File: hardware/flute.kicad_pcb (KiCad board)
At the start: 2 copper layers, 280 x 20 mm, 30 parts, among them J1 Conn_01x04, SW1 C, SW2 D, SW3 E, SW4 F, SW5 G, SW6 A, SW7 H, SW8 OCTAVE?, U1 W25Q128JVS, Y1 Crystal_GND24

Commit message: Update flute.kicad_pcb
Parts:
- MIC.CASE1: moved to B.Cu
- moved MIC.CASE1 57.4 mm to (73.5, 101.5), turned to -90 degrees
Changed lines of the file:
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@@
 		)
 	)
-	(footprint "Resistor_THT:R_Axial_DIN0204_L3.6mm_D1.6mm_P2.54mm_Vertical"
-		(layer "F.Cu")
-		(at 61.695 45.36)
-		(descr "Resistor, Axial_DIN0204 series, Axial, Vertical, pin pitch=2.54mm, 0.167W, length*diameter=3.6*1.6mm^2, http://cdn-reichelt.de/documents/datenblatt/B400/1_4W%23YAG.pdf")
-		(tags "Resistor Axial_DIN0204 series Axial Vertical pin pitch 2.54mm 0.167W length 3.6mm diameter 1.6mm")
-		(property "Reference" "MIC.CASE1"
-			(at 1.27 -1.92 0)
-			(layer "F.SilkS")
-			(effects
-				(font
-					(size 1 1)
-					(thickness 0.15)
-				)
-			)
-		)
-		(property "Value" "R"
-			(at 1.27 1.92 0)
-			(layer "F.Fab")
-			(effects
-				(font
-					(size 1 1)
-					(thickness 0.15)
-				)
-			)
-		)
-		(property "Datasheet" "~"
-			(at 0 0 0)
-			(layer "F.Fab")
-			(hide yes)
-			(effects
-				(font
-					(size 1.27 1.27)
-					(thickness 0.15)
-				)
-			)
-		)
-		(property "Description" "Resistor"
-			(at 0 0 0)
-			(layer "F.Fab")
-			(hide yes)
-			(effects
-				(font
-					(size 1.27 1.27)
-					(thickness 0.15)
-				)
-			)
-		)
-		(property ki_fp_filters "R_*")
-		(sheetname "/MICROPHONE/")
-		(sheetfile "./microphone.kicad_sch")
-		(attr through_hole)
-		(fp_line
-			(start 0.92 0)
-			(end 1.54 0)
-			(stroke
-				(width 0.12)
-				(type solid)
-			)
-			(layer "F.SilkS")
-		)
-		(fp_circle
-			(center 0 0)
-			(end 0.92 0)
-			(stroke
-				(width 0.12)
-				(type solid)
-			)
-			(fill no)
-			(layer "F.SilkS")
-		)
-		(fp_rect
-			(start -1.05 -1.05)
-			(end 3.49 1.05)
-			(stroke
-				(width 0.05)
-				(type solid)
-			)
-			(fill no)
-			(layer "F.CrtYd")
-		)
-		(fp_line
-			(start 0 0)
-			(end 2.54 0)
-			(stroke
-				(width 0.1)
-				(type solid)
-			)
-			(layer "F.Fab")
-		)
-		(fp_circle
-			(center 0 0)
-			(end 0.8 0)
-			(stroke
-				(width 0.1)
-				(type solid)
-			)
-			(fill no)
-			(layer "F.Fab")
-		)
-		(fp_text user "${REFERENCE}"
-			(at 1.27 -1.92 0)
-			(layer "F.Fab")
-			(effects
-				(font
-					(size 1 1)
-					(thickness 0.15)
-				)
-			)
-		)
-		(pad "1" thru_hole circle
-			(at 0 0)
-			(size 1.4 1.4)
-			(drill 0.7)
-			(layers "*.Cu" "*.Mask")
-			(remove_unused_layers no)
-			(net 3 "GND")
-			(pintype "passive")
-		)
-		(pad "2" thru_hole circle
-			(at 2.54 0)
-			(size 1.4 1.4)
-			(drill 0.7)
-			(layers "*.Cu" "*.Mask")
-			(remove_unused_layers no)
-			(net 2 "Net-(C1-Pad1)")
-			(pintype "passive")
-		)
-		(embedded_fonts no)
-		(model "${KICAD9_3DMODEL_DIR}/Resistor_THT.3dshapes/R_Axial_DIN0204_L3.6mm_D1.6mm_P2.54mm_Vertical.step"
-			(offset
-				(xyz 0 0 0)
-			)
-			(scale
-				(xyz 1 1 1)
-			)
-			(rotate
-				(xyz 0 0 0)
-			)
-		)
-	)
 	(footprint "Button_Switch_SMD:SW_SPST_Omron_B3FS-100xP"
 		(layer "F.Cu")
@@
 			(offset
 				(xyz 0 0 0)
+			)
+			(scale
+				(xyz 1 1 1)
+			)
+			(rotate
+				(xyz 0 0 0)
+			)
+		)
+	)
+	(footprint "Resistor_THT:R_Axial_DIN0204_L3.6mm_D1.6mm_P2.54mm_Vertical"
+		(layer "B.Cu")
+		(at 73.46 101.5 -90)
+		(descr "Resistor, Axial_DIN0204 series, Axial, Vertical, pin pitch=2.54mm, 0.167W, length*diameter=3.6*1.6mm^2, http://cdn-reichelt.de/documents/datenblatt/B400/1_4W%23YAG.pdf")
+		(tags "Resistor Axial_DIN0204 series Axial Vertical pin pitch 2.54mm 0.167W length 3.6mm diameter 1.6mm")
+		(property "Reference" "MIC.CASE1"
+			(at 1.27 1.92 90)
+			(layer "B.SilkS")
+			(effects
+				(font
+					(size 1 1)
+					(thickness 0.15)
+				)
+				(justify mirror)
+			)
+		)
+		(property "Value" "R"
+			(at 1.27 -1.92 90)
+			(layer "B.Fab")
+			(effects
+				(font
+					(size 1 1)
+					(thickness 0.15)
+				)
+				(justify mirror)
+			)
+		)
+		(property "Datasheet" "~"
+			(at 0 0 90)
+			(layer "B.Fab")
+			(hide yes)
+			(effects
+				(font
+					(size 1.27 1.27)
+					(thickness 0.15)
+				)
+				(justify mirror)
+			)
+		)
+		(property "Description" "Resistor"
+			(at 0 0 90)
+			(layer "B.Fab")
+			(hide yes)
+			(effects
+				(font
+					(size 1.27 1.27)
+					(thickness 0.15)
+				)
+				(justify mirror)
+			)
+		)
+		(property ki_fp_filters "R_*")
+		(sheetname "/MICROPHONE/")
+		(sheetfile "./microphone.kicad_sch")
+		(attr through_hole)
+		(fp_line
+			(start 0.92 0)
+			(end 1.54 0)
+			(stroke
+				(width 0.12)
+				(type solid)
+			)
+			(layer "B.SilkS")
+		)
+		(fp_circle
+			(center 0 0)
+			(end 0.92 0)
+			(stroke
+				(width 0.12)
+				(type solid)
+			)
+			(fill no)
+			(layer "B.SilkS")
+		)
+		(fp_rect
+			(start -1.05 1.05)
+			(end 3.49 -1.05)
+			(stroke
+				(width 0.05)
+				(type solid)
+			)
+			(fill no)
+			(layer "B.CrtYd")
+		)
+		(fp_line
+			(start 0 0)
+			(end 2.54 0)
+			(stroke
+				(width 0.1)
+				(type solid)
+			)
+			(layer "B.Fab")
+		)
+		(fp_circle
+			(center 0 0)
+			(end 0.8 0)
+			(stroke
+				(width 0.1)
+				(type solid)
+			)
+			(fill no)
+			(layer "B.Fab")
+		)
+		(fp_text user "${REFERENCE}"
+			(at 1.27 1.92 90)
+			(layer "B.Fab")
+			(effects
+				(font
+					(size 1 1)
+					(thickness 0.15)
+				)
+				(justify mirror)
+			)
+		)
+		(pad "1" thru_hole circle
+			(at 0 0 270)
+			(size 1.4 1.4)
+			(drill 0.7)
+			(layers "*.Cu" "*.Mask")
+			(remove_unused_layers no)
+			(net 3 "GND")
+			(pintype "passive")
+		)
+		(pad "2" thru_hole circle
+			(at 2.54 0 270)
+			(size 1.4 1.4)
+			(drill 0.7)
+			(layers "*.Cu" "*.Mask")
+			(remove_unused_layers no)
+			(net 2 "Net-(C1-Pad1)")
+			(pintype "passive")
+		)
+		(embedded_fonts no)
+		(model "${KICAD9_3DMODEL_DIR}/Resistor_THT.3dshapes/R_Axial_DIN0204_L3.6mm_D1.6mm_P2.54mm_Vertical.step"
+			(offset
+				(xyz 0 0 0)

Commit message: Update flute.kicad_pcb
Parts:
- moved C1 82.5 mm to (67.0, 130.2), turned to 90 degrees
- moved R1 82.2 mm to (67.7, 131.5)
- moved MIC.CASE1 28.6 mm to (65.5, 129.0)
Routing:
- net Net-(C1-Pad1): track 0.00 -> 3.02 mm
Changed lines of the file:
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@@
 	(footprint "Resistor_SMD:R_0201_0603Metric"
 		(layer "F.Cu")
-		(at 61.345 49.56)
+		(at 67.655 131.5)
 		(descr "Resistor SMD 0201 (0603 Metric), square (rectangular) end terminal, IPC-7351 nominal, (Body size source: https://www.vishay.com/docs/20052/crcw0201e3.pdf), generated with kicad-footprint-generator")
 		(tags "resistor")
@@
 	(footprint "Capacitor_SMD:C_0201_0603Metric"
 		(layer "F.Cu")
-		(at 61.345 47.81)
+		(at 67 130.155 90)
 		(descr "Capacitor SMD 0201 (0603 Metric), square (rectangular) end terminal, IPC-7351 nominal, (Body size source: https://www.vishay.com/docs/20052/crcw0201e3.pdf), generated with kicad-footprint-generator")
 		(tags "capacitor")
 		(property "Reference" "C1"
-			(at 0 -1.05 0)
+			(at 0 -1.05 90)
 			(layer "F.SilkS")
 			(effects
@@
 		)
 		(property "Value" "1uF"
-			(at 0 1.05 0)
+			(at 0 1.05 90)
 			(layer "F.Fab")
 			(effects
@@
 		)
 		(property "Datasheet" "~"
-			(at 0 0 0)
+			(at 0 0 90)
 			(layer "F.Fab")
 			(hide yes)
@@
 		)
 		(property "Description" "Unpolarized capacitor"
-			(at 0 0 0)
+			(at 0 0 90)
 			(layer "F.Fab")
 			(hide yes)
@@
 		(attr smd)
 		(fp_line
+			(start 0.7 -0.35)
+			(end 0.7 0.35)
+			(stroke
+				(width 0.05)
+				(type solid)
+			)
+			(layer "F.CrtYd")
+		)
+		(fp_line
 			(start -0.7 -0.35)
 			(end 0.7 -0.35)
@@
 		)
 		(fp_line
+			(start 0.7 0.35)
+			(end -0.7 0.35)
+			(stroke
+				(width 0.05)
+				(type solid)
+			)
+			(layer "F.CrtYd")
+		)
+		(fp_line
 			(start -0.7 0.35)
 			(end -0.7 -0.35)
@@
 		)
 		(fp_line
-			(start 0.7 -0.35)
-			(end 0.7 0.35)
-			(stroke
-				(width 0.05)
-				(type solid)
-			)
-			(layer "F.CrtYd")
-		)
-		(fp_line
-			(start 0.7 0.35)
-			(end -0.7 0.35)
-			(stroke
-				(width 0.05)
-				(type solid)
-			)
-			(layer "F.CrtYd")
+			(start 0.3 -0.15)
+			(end 0.3 0.15)
+			(stroke
+				(width 0.1)
+				(type solid)
+			)
+			(layer "F.Fab")
 		)
 		(fp_line
@@
 		)
 		(fp_line
+			(start 0.3 0.15)
+			(end -0.3 0.15)
+			(stroke
+				(width 0.1)
+				(type solid)
+			)
+			(layer "F.Fab")
+		)
+		(fp_line
 			(start -0.3 0.15)
 			(end -0.3 -0.15)
@@
 			(layer "F.Fab")
 		)
-		(fp_line
-			(start 0.3 -0.15)
-			(end 0.3 0.15)
-			(stroke
-				(width 0.1)
-				(type solid)
-			)
-			(layer "F.Fab")
-		)
-		(fp_line
-			(start 0.3 0.15)
-			(end -0.3 0.15)
-			(stroke
-				(width 0.1)
-				(type solid)
-			)
-			(layer "F.Fab")
-		)
 		(fp_text user "${REFERENCE}"
-			(at 0 -0.68 0)
+			(at 0 -0.68 90)
 			(layer "F.Fab")
 			(effects
@@
 		)
 		(pad "" smd roundrect
-			(at -0.345 0)
+			(at -0.345 0 90)
 			(size 0.318 0.36)
 			(layers "F.Paste")
@@
 		)
 		(pad "" smd roundrect
-			(at 0.345 0)
+			(at 0.345 0 90)
 			(size 0.318 0.36)
 			(layers "F.Paste")
@@
 		)
 		(pad "1" smd roundrect
-			(at -0.32 0)
+			(at -0.32 0 90)
 			(size 0.46 0.4)
 			(layers "F.Cu" "F.Mask")
@@
 		)
 		(pad "2" smd roundrect
-			(at 0.32 0)
+			(at 0.32 0 90)
 			(size 0.46 0.4)
 			(layers "F.Cu" "F.Mask")
@@
 	(footprint "Resistor_THT:R_Axial_DIN0204_L3.6mm_D1.6mm_P2.54mm_Vertical"
 		(layer "B.Cu")
-		(at 73.46 101.5 -90)
+		(at 65.5 129 -90)
 		(descr "Resistor, Axial_DIN0204 series, Axial, Vertical, pin pitch=2.54mm, 0.167W, length*diameter=3.6*1.6mm^2, http://cdn-reichelt.de/documents/datenblatt/B400/1_4W%23YAG.pdf")
 		(tags "Resistor Axial_DIN0204 series Axial Vertical pin pitch 2.54mm 0.167W length 3.6mm diameter 1.6mm")
@@
 		(layer "Edge.Cuts")
 	)
+	(segment
+		(start 67.295 131.54)
+		(end 67.335 131.5)
+		(width 0.2)
+		(layer "F.Cu")
+		(net 2)
+	)
+	(segment
+		(start 65.5 131.54)
+		(end 67.295 131.54)
+		(width 0.2)
+		(layer "F.Cu")
+		(net 2)
+	)
+	(segment
+		(start 67 131.165)
+		(end 67.335 131.5)
+		(width 0.2)
+		(layer "F.Cu")
+		(net 2)
+	)
+	(segment
+		(start 67 130.475)
+		(end 67 131.165)
+		(width 0.2)
+		(layer "F.Cu")
+		(net 2)
+	)
 	(embedded_fonts no)

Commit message: r and c footprint change
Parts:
- C1: footprint Capacitor_SMD:C_0201_0603Metric -> Capacitor_SMD:C_0603_1608Metric
- R1: value 1k -> 1K; footprint Resistor_SMD:R_0201_0603Metric -> Resistor_SMD:R_0603_1608Metric
- moved C1 0.98 mm to (67.6, 129.4)
- moved R1 0.80 mm to (68.4, 131.8), turned to 180 degrees
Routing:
- net Net-(C1-Pad1): track 3.02 -> 5.00 mm

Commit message: minor schematic changes
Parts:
- C10, C11, C12, C13, C14, C15, C2, C3, C4, C5, C6, C7, C8, C9: footprint Capacitor_SMD:C_0201_0603Metric -> Capacitor_SMD:C_0603_1608Metric
- SW1: footprint Button_Switch_SMD:SW_SPST_PTS647_Sx38 -> Button_Switch_THT:SW_TH_Tactile_Omron_B3F-100x
- SW2, SW3, SW4, SW5, SW6, SW7, SW8: footprint Button_Switch_SMD:SW_SPST_Omron_B3FS-100xP -> Button_Switch_THT:SW_TH_Tactile_Omron_B3F-100x
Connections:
- net /RASPBERRY_PI_PICO/GPIO0 renamed GPIO0
- net /RASPBERRY_PI_PICO/GPIO1 renamed GPIO1
- net /RASPBERRY_PI_PICO/GPIO10 renamed GPIO10
- net /RASPBERRY_PI_PICO/GPIO12 renamed GPIO12
- net /RASPBERRY_PI_PICO/GPIO13 renamed GPIO13
- net /RASPBERRY_PI_PICO/GPIO14 renamed GPIO14
- net /RASPBERRY_PI_PICO/GPIO15 renamed GPIO15
- net /RASPBERRY_PI_PICO/GPIO16 renamed GPIO16
- net /RASPBERRY_PI_PICO/GPIO17 renamed GPIO17
- net /RASPBERRY_PI_PICO/GPIO18 renamed GPIO18
- net /RASPBERRY_PI_PICO/GPIO19 renamed GPIO19
- net /RASPBERRY_PI_PICO/GPIO20 renamed GPIO20
- net /RASPBERRY_PI_PICO/GPIO21 renamed GPIO21
- net /RASPBERRY_PI_PICO/GPIO22 renamed GPIO22
- net /RASPBERRY_PI_PICO/GPIO23 renamed GPIO23
- net /RASPBERRY_PI_PICO/GPIO24 renamed GPIO24
- net /RASPBERRY_PI_PICO/GPIO25 renamed GPIO25
- net /RASPBERRY_PI_PICO/GPIO26 renamed GPIO26
- net /RASPBERRY_PI_PICO/GPIO27 renamed GPIO27
- net /RASPBERRY_PI_PICO/GPIO28 renamed GPIO28
- net /RASPBERRY_PI_PICO/GPIO29 renamed GPIO29
- C1 pad 2: /MICROPHONE/GPIO11 -> GPIO11
- RASPBERRY_PI1 pad 1: Net-(RASPBERRY_PI1-ADC_AVDD) -> +3V3
- RASPBERRY_PI1 pad 10: Net-(RASPBERRY_PI1-ADC_AVDD) -> +3V3
- RASPBERRY_PI1 pad 11: /RASPBERRY_PI_PICO/GPIO8 -> GPIO8
- RASPBERRY_PI1 pad 12: /RASPBERRY_PI_PICO/GPIO9 -> GPIO9
- RASPBERRY_PI1 pad 14: /RASPBERRY_PI_PICO/GPIO11 -> GPIO11
- RASPBERRY_PI1 pad 22: Net-(RASPBERRY_PI1-ADC_AVDD) -> +3V3
- RASPBERRY_PI1 pad 33: Net-(RASPBERRY_PI1-ADC_AVDD) -> +3V3
- RASPBERRY_PI1 pad 4: /RASPBERRY_PI_PICO/GPIO2 -> GPIO2
- RASPBERRY_PI1 pad 42: Net-(RASPBERRY_PI1-ADC_AVDD) -> +3V3
- RASPBERRY_PI1 pad 43: Net-(RASPBERRY_PI1-ADC_AVDD) -> +3V3
- RASPBERRY_PI1 pad 44: Net-(RASPBERRY_PI1-ADC_AVDD) -> +3V3
- RASPBERRY_PI1 pad 48: Net-(RASPBERRY_PI1-ADC_AVDD) -> +3V3
- RASPBERRY_PI1 pad 49: Net-(RASPBERRY_PI1-ADC_AVDD) -> +3V3
- RASPBERRY_PI1 pad 5: /RASPBERRY_PI_PICO/GPIO3 -> GPIO3
- RASPBERRY_PI1 pad 6: /RASPBERRY_PI_PICO/GPIO4 -> GPIO4
- RASPBERRY_PI1 pad 7: /RASPBERRY_PI_PICO/GPIO5 -> GPIO5
- RASPBERRY_PI1 pad 8: /RASPBERRY_PI_PICO/GPIO6 -> GPIO6
- RASPBERRY_PI1 pad 9: /RASPBERRY_PI_PICO/GPIO7 -> GPIO7
- SW1 pad 2: /BUTTONS/GPIO2 -> GPIO2
- SW2 pad 2: /BUTTONS/GPIO3 -> GPIO3
- SW3 pad 2: /BUTTONS/GPIO4 -> GPIO4
- SW4 pad 2: /BUTTONS/GPIO5 -> GPIO5
- SW5 pad 2: /BUTTONS/GPIO6 -> GPIO6
- SW6 pad 2: /BUTTONS/GPIO7 -> GPIO7
- SW7 pad 2: /BUTTONS/GPIO8 -> GPIO8
- SW8 pad 2: /BUTTONS/GPIO9 -> GPIO9

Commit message: raspberry pi pcb
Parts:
- added C6: 1uF, Capacitor_SMD:C_0603_1608Metric, F.Cu at (89.4, 128.4)
- added R3: 100k, Resistor_SMD:R_0603_1608Metric, F.Cu at (89.5, 126.6)
- J1: footprint Connector_PinHeader_2.54mm:PinHeader_1x04_P2.54mm_Vertical -> Connector_PinHeader_2.54mm:PinHeader_2x02_P2.54mm_Vertical
- R2: footprint Resistor_SMD:R_0201_0603Metric -> Resistor_SMD:R_0603_1608Metric
- moved SW8 232.6 mm to (284.0, 133.8), turned to 180 degrees
- moved SW7 224.4 mm to (255.1, 128.6)
- moved SW6 201.2 mm to (238.3, 128.6)
- moved SW5 191.5 mm to (221.0, 128.5)
- moved SW4 184.9 mm to (207.6, 128.8)
- moved SW3 177.4 mm to (194.6, 128.7)
- moved SW2 170.1 mm to (180.0, 129.0)
- moved SW1 151.6 mm to (165.1, 129.0)
- moved Y1 113.6 mm to (79.5, 138.4)
- moved C2 107.5 mm to (84.2, 137.0), turned to 90 degrees
- moved J1 107.0 mm to (88.9, 138.4), turned to 90 degrees
- moved C4 104.9 mm to (76.6, 138.7), turned to 90 degrees
- moved C5 104.5 mm to (83.3, 139.4)
- moved R2 103.4 mm to (82.5, 137.1), turned to -90 degrees
- moved C8 100.6 mm to (85.9, 138.7), turned to -90 degrees
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- renumbered C9 to C10, C10 to C11, C11 to C12, C12 to C13, C13 to C14, C14 to C15, C15 to C16, C6 to C7, C7 to C8, C8 to C9
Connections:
- C3 pad 1: unconnected-(C3-Pad1) -> +3V3
- RASPBERRY_PI1 pad 41: GPIO29 -> Net-(RASPBERRY_PI1-GPIO29_ADC3)
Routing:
- net +3V3: track 0.00 -> 37.0 mm, vias 0 -> 2
- net +1V1: track 0.00 -> 19.0 mm
- net GPIO11: track 0.00 -> 14.1 mm
- net /RASPBERRY_PI_PICO/QSPI_SD1: track 0.00 -> 9.99 mm, vias 0 -> 1
- net /RASPBERRY_PI_PICO/QSPI_CS: track 0.00 -> 9.93 mm
- net /RASPBERRY_PI_PICO/XIN: track 0.00 -> 9.23 mm
- net /RASPBERRY_PI_PICO/RUN: track 0.00 -> 8.56 mm
- net /RASPBERRY_PI_PICO/SWCLK: track 0.00 -> 7.36 mm
- net /RASPBERRY_PI_PICO/SWDIO: track 0.00 -> 6.11 mm, vias 0 -> 1
- net /RASPBERRY_PI_PICO/QSPI_SD3: track 0.00 -> 5.62 mm, vias 0 -> 1
- net /RASPBERRY_PI_PICO/QSPI_SCLK: track 0.00 -> 4.34 mm
- net Net-(C5-Pad1): track 0.00 -> 3.59 mm
- net /RASPBERRY_PI_PICO/QSPI_SD0: track 0.00 -> 2.74 mm
- net GPIO29: track 0.00 -> 2.42 mm
- net /RASPBERRY_PI_PICO/XOUT: track 0.00 -> 2.34 mm
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
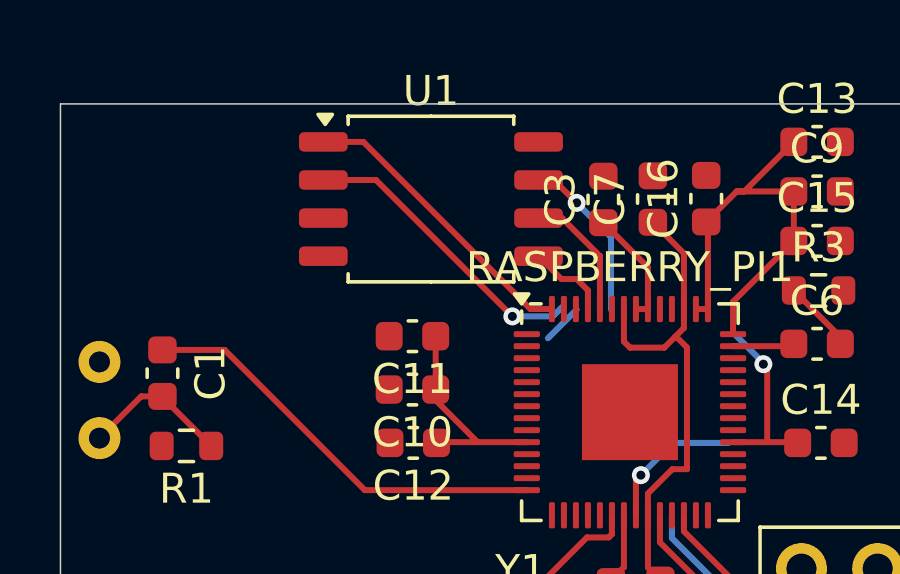
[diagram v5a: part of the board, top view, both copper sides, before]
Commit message: added missing connection to QSPI_SD2
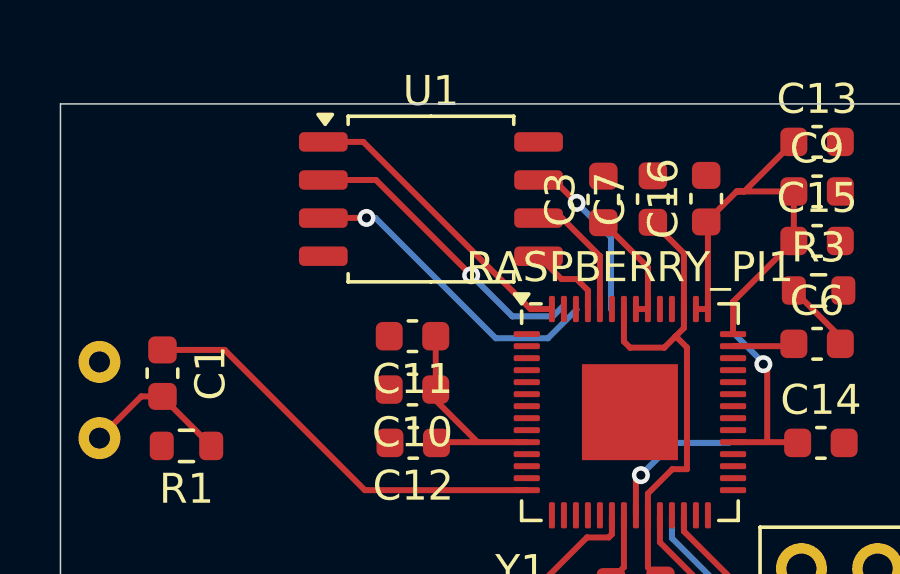
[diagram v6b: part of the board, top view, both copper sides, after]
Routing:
- net /RASPBERRY_PI_PICO/QSPI_SD2: track 1.35 -> 10.5 mm, vias 0 -> 1
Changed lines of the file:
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@@
 	(segment
 		(start 74.716473 122.936)
-		(end 79.262975 127.482502)
+		(end 72.962 122.936)
 		(width 0.2)
 		(layer "F.Cu")
@@
 	)
 	(segment
-		(start 72.962 122.936)
+		(start 77.890236 126.109764)
 		(end 74.716473 122.936)
 		(width 0.2)
@@
 	)
 	(via
-		(at 79.262975 127.482502)
+		(at 77.890236 126.109764)
 		(size 0.6)
 		(drill 0.3)
@@
 	)
 	(segment
-		(start 80.93295 127.16095)
+		(start 77.890236 126.109764)
+		(end 79.262974 127.482502)
+		(width 0.2)
+		(layer "B.Cu")
+		(net 21)
+	)
+	(segment
+		(start 79.262974 127.482502)
 		(end 80.611398 127.482502)
 		(width 0.2)
@@
 	(segment
 		(start 80.611398 127.482502)
-		(end 79.262975 127.482502)
+		(end 80.93295 127.16095)
 		(width 0.2)
 		(layer "B.Cu")
@@
 	)
 	(segment
+		(start 72.968 124.2)
+		(end 72.962 124.206)
+		(width 0.2)
+		(layer "F.Cu")
+		(net 44)
+	)
+	(segment
+		(start 74.4 124.2)
+		(end 72.968 124.2)
+		(width 0.2)
+		(layer "F.Cu")
+		(net 44)
+	)
+	(via
+		(at 74.4 124.2)
+		(size 0.6)
+		(drill 0.3)
+		(layers "F.Cu" "B.Cu")
+		(net 44)
+	)
+	(segment
 		(start 80.448896 128.212104)
-		(end 81.407 127.254)
+		(end 78.712104 128.212104)
 		(width 0.2)
 		(layer "B.Cu")
+		(net 44)
+	)
+	(segment
+		(start 81.407 127.254)
+		(end 80.448896 128.212104)
+		(width 0.2)
+		(layer "B.Cu")
+		(net 44)
+	)
+	(segment
+		(start 74.7 124.2)
+		(end 74.4 124.2)
+		(width 0.2)
+		(layer "B.Cu")
+		(net 44)
+	)
+	(segment
+		(start 78.712104 128.212104)
+		(end 74.7 124.2)
+		(width 0.2)
+		(layer "B.Cu")

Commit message: aligned button + new pcb outline
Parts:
- moved SW8 159.5 mm to (124.5, 132.7)
- moved SW1 62.4 mm to (102.8, 128.2)
- moved SW2 46.7 mm to (133.3, 128.2)
- moved SW7 30.9 mm to (286.0, 128.2)
- moved SW3 30.7 mm to (163.8, 128.2)
- moved SW6 17.2 mm to (255.5, 128.2)
- moved SW4 13.3 mm to (194.4, 128.2)
- moved SW5 3.90 mm to (224.9, 128.2)
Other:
- board size 280 x 20 mm -> 230 x 20 mm
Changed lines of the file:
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@@
 	(footprint "Button_Switch_THT:SW_TH_Tactile_Omron_B3F-100x"
 		(layer "F.Cu")
-		(at 207.645 128.85)
+		(at 194.375 128.15)
 		(descr "Tactile switch, 6x6 mm, H4.3 mm, 6.5 mm pitch, https://omronfs.omron.com/en_US/ecb/products/pdf/en-b3f.pdf")
 		(tags "Omron B3F-10xx SPST 1P1T")
@@
 	(footprint "Button_Switch_THT:SW_TH_Tactile_Omron_B3F-100x"
 		(layer "F.Cu")
-		(at 238.252 128.596)
+		(at 255.458333 128.15)
 		(descr "Tactile switch, 6x6 mm, H4.3 mm, 6.5 mm pitch, https://omronfs.omron.com/en_US/ecb/products/pdf/en-b3f.pdf")
 		(tags "Omron B3F-10xx SPST 1P1T")
@@
 	(footprint "Button_Switch_THT:SW_TH_Tactile_Omron_B3F-100x"
 		(layer "F.Cu")
-		(at 165.1 128.977)
+		(at 102.75 128.15)
 		(descr "Tactile switch, 6x6 mm, H4.3 mm, 6.5 mm pitch, https://omronfs.omron.com/en_US/ecb/products/pdf/en-b3f.pdf")
 		(tags "Omron B3F-10xx SPST 1P1T")
@@
 	(footprint "Button_Switch_THT:SW_TH_Tactile_Omron_B3F-100x"
 		(layer "F.Cu")
-		(at 284.047 133.822 180)
+		(at 124.520834 132.65 180)
 		(descr "Tactile switch, 6x6 mm, H4.3 mm, 6.5 mm pitch, https://omronfs.omron.com/en_US/ecb/products/pdf/en-b3f.pdf")
 		(tags "Omron B3F-10xx SPST 1P1T")
@@
 	(footprint "Button_Switch_THT:SW_TH_Tactile_Omron_B3F-100x"
 		(layer "F.Cu")
-		(at 194.564 128.723)
+		(at 163.833333 128.15)
 		(descr "Tactile switch, 6x6 mm, H4.3 mm, 6.5 mm pitch, https://omronfs.omron.com/en_US/ecb/products/pdf/en-b3f.pdf")
 		(tags "Omron B3F-10xx SPST 1P1T")
@@
 	(footprint "Button_Switch_THT:SW_TH_Tactile_Omron_B3F-100x"
 		(layer "F.Cu")
-		(at 221.032 128.505)
+		(at 224.916667 128.15)
 		(descr "Tactile switch, 6x6 mm, H4.3 mm, 6.5 mm pitch, https://omronfs.omron.com/en_US/ecb/products/pdf/en-b3f.pdf")
 		(tags "Omron B3F-10xx SPST 1P1T")
@@
 	(footprint "Button_Switch_THT:SW_TH_Tactile_Omron_B3F-100x"
 		(layer "F.Cu")
-		(at 255.143 128.596)
+		(at 286 128.15)
 		(descr "Tactile switch, 6x6 mm, H4.3 mm, 6.5 mm pitch, https://omronfs.omron.com/en_US/ecb/products/pdf/en-b3f.pdf")
 		(tags "Omron B3F-10xx SPST 1P1T")
@@
 	(footprint "Button_Switch_THT:SW_TH_Tactile_Omron_B3F-100x"
 		(layer "F.Cu")
-		(at 180.011 129.013)
+		(at 133.291667 128.15)
 		(descr "Tactile switch, 6x6 mm, H4.3 mm, 6.5 mm pitch, https://omronfs.omron.com/en_US/ecb/products/pdf/en-b3f.pdf")
 		(tags "Omron B3F-10xx SPST 1P1T")
@@
 	(gr_rect
 		(start 64.2 120.4)
-		(end 344.2 140.4)
+		(end 294.2 140.4)
 		(stroke
 			(width 0.05)
